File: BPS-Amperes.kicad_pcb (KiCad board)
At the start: 2 copper layers, 40 x 50 mm, 35 parts, among them J1 Conn_02x10_Odd_Even, J2 ShuntConn, J3 PassthroughConn, J4 TestConn, J5 Conn_01x02, U1 INA186A3IDDFT, U2 OPA2196, U4 REF1930AIDDCT

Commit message: Manthan Suggestions
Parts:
- turned C10 to 180 degrees
- turned C9 to 180 degrees
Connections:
- net /5V_Ext renamed /PA2
- net /Aout renamed /PA1
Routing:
- added copper zone on B.Cu, net GND
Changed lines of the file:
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@@
   (net 15 "/SPI1_MOSI")
   (net 16 "/SPI1_NSS")
-  (net 17 "/5V_Ext")
-  (net 18 "/Aout")
+  (net 17 "/PA1")
+  (net 18 "/PA2")
   (net 19 "+3V0")
   (net 20 "/RSHH")
@@
       (net 15 "/SPI1_MOSI") (pinfunction "Pin_17") (pintype "passive+no_connect"))
     (pad "18" smd rect locked (at -2.8 2.15 90) (size 0.55 1.8) (layers "F.Cu" "F.Paste" "F.Mask")
-      (net 17 "/5V_Ext") (pinfunction "Pin_18") (pintype "passive+no_connect"))
+      (net 18 "/PA2") (pinfunction "Pin_18") (pintype "passive+no_connect"))
     (pad "19" smd rect locked (at -3.6 -2.15 90) (size 0.55 1.8) (layers "F.Cu" "F.Paste" "F.Mask")
       (net 16 "/SPI1_NSS") (pinfunction "Pin_19") (pintype "passive+no_connect"))
     (pad "20" smd rect locked (at -3.6 2.15 90) (size 0.55 1.8) (layers "F.Cu" "F.Paste" "F.Mask")
-      (net 18 "/Aout") (pinfunction "Pin_20") (pintype "passive"))
+      (net 17 "/PA1") (pinfunction "Pin_20") (pintype "passive"))
     (model "${KIPRJMOD}/common/utsvt3d/connectors.3dshapes/53307-2071.stp"
       (offset (xyz 0 0 1.849999996))
@@
     (descr "Diode SMD 0805 (2012 Metric), square (rectangular) end terminal, IPC_7351 nominal, (Body size source: https://docs.google.com/spreadsheets/d/1BsfQQcO9C6DZCsRaXUlFlo91Tg2WpOkGARC1WS5S8t0/edit?usp=sharing), generated with kicad-footprint-generator")
     (tags "diode")
-    (property "Mfg" "BZX38450-C3V0X")
+    (property "Mfg" "821-BZY55B3V3RBG")
     (property "Sheetfile" "BPS-Amperes.kicad_sch")
     (property "Sheetname" "")
@@
       (stroke (width 0.1) (type solid)) (layer "B.Fab"))
     (pad "1" smd roundrect (at -0.9375 0 90) (size 0.975 1.4) (layers "B.Cu" "B.Paste" "B.Mask") (roundrect_rratio 0.25)
-      (net 18 "/Aout") (pinfunction "K") (pintype "passive"))
+      (net 17 "/PA1") (pinfunction "K") (pintype "passive"))
     (pad "2" smd roundrect (at 0.9375 0 90) (size 0.975 1.4) (layers "B.Cu" "B.Paste" "B.Mask") (roundrect_rratio 0.25)
       (net 4 "GND") (pinfunction "A") (pintype "passive"))
@@
   )
   (footprint "Capacitor_SMD:C_0805_2012Metric" (layer "B.Cu")
-    (at 146.2125 97.435)
+    (at 146.2125 97.435 180)
     (descr "Capacitor SMD 0805 (2012 Metric), square (rectangular) end terminal, IPC_7351 nominal, (Body size source: IPC-SM-782 page 76, https://www.pcb-3d.com/wordpress/wp-content/uploads/ipc-sm-782a_amendment_1_and_2.pdf, https://docs.google.com/spreadsheets/d/1BsfQQcO9C6DZCsRaXUlFlo91Tg2WpOkGARC1WS5S8t0/edit?usp=sharing), generated with kicad-footprint-generator")
     (tags "capacitor")
@@
     (property "ki_keywords" "capacitor cap")
     (attr smd)
-    (fp_text reference "C9" (at 2.4375 0.065) (layer "B.SilkS")
+    (fp_text reference "C9" (at -3.2875 0.065) (layer "B.SilkS")
         (effects (font (size 1 1) (thickness 0.15)) (justify mirror))
     )
@@
     (fp_line (start 1 0.625) (end 1 -0.625)
       (stroke (width 0.1) (type solid)) (layer "B.Fab"))
-    (pad "1" smd roundrect (at -0.95 0) (size 1 1.45) (layers "B.Cu" "B.Paste" "B.Mask") (roundrect_rratio 0.25)
+    (pad "1" smd roundrect (at -0.95 0 180) (size 1 1.45) (layers "B.Cu" "B.Paste" "B.Mask") (roundrect_rratio 0.25)
       (net 25 "+1V5") (pintype "passive"))
-    (pad "2" smd roundrect (at 0.95 0) (size 1 1.45) (layers "B.Cu" "B.Paste" "B.Mask") (roundrect_rratio 0.25)
+    (pad "2" smd roundrect (at 0.95 0 180) (size 1 1.45) (layers "B.Cu" "B.Paste" "B.Mask") (roundrect_rratio 0.25)
       (net 4 "GND") (pintype "passive"))
     (model "${KICAD6_3DMODEL_DIR}/Capacitor_SMD.3dshapes/C_0805_2012Metric.wrl"
@@
   )
   (footprint "Capacitor_SMD:C_0805_2012Metric" (layer "B.Cu")
-    (at 146.2125 100)
+    (at 146.2125 100 180)
     (descr "Capacitor SMD 0805 (2012 Metric), square (rectangular) end terminal, IPC_7351 nominal, (Body size source: IPC-SM-782 page 76, https://www.pcb-3d.com/wordpress/wp-content/uploads/ipc-sm-782a_amendment_1_and_2.pdf, https://docs.google.com/spreadsheets/d/1BsfQQcO9C6DZCsRaXUlFlo91Tg2WpOkGARC1WS5S8t0/edit?usp=sharing), generated with kicad-footprint-generator")
     (tags "capacitor")
@@
     (property "ki_keywords" "capacitor cap")
     (attr smd)
-    (fp_text reference "C10" (at 2.9375 0) (layer "B.SilkS")
+    (fp_text reference "C10" (at -3.7875 0) (layer "B.SilkS")
         (effects (font (size 1 1) (thickness 0.15)) (justify mirror))
     )
@@
     (fp_line (start 1 0.625) (end 1 -0.625)
       (stroke (width 0.1) (type solid)) (layer "B.Fab"))
-    (pad "1" smd roundrect (at -0.95 0) (size 1 1.45) (layers "B.Cu" "B.Paste" "B.Mask") (roundrect_rratio 0.25)
+    (pad "1" smd roundrect (at -0.95 0 180) (size 1 1.45) (layers "B.Cu" "B.Paste" "B.Mask") (roundrect_rratio 0.25)
       (net 25 "+1V5") (pintype "passive"))
-    (pad "2" smd roundrect (at 0.95 0) (size 1 1.45) (layers "B.Cu" "B.Paste" "B.Mask") (roundrect_rratio 0.25)
+    (pad "2" smd roundrect (at 0.95 0 180) (size 1 1.45) (layers "B.Cu" "B.Paste" "B.Mask") (roundrect_rratio 0.25)
       (net 4 "GND") (pintype "passive"))
     (model "${KICAD6_3DMODEL_DIR}/Capacitor_SMD.3dshapes/C_0805_2012Metric.wrl"
@@
       (net 32 "Net-(U2B--)") (pintype "passive"))
     (pad "2" smd roundrect (at 0.9125 0) (size 1.025 1.4) (layers "B.Cu" "B.Paste" "B.Mask") (roundrect_rratio 0.243902)
-      (net 18 "/Aout") (pintype "passive"))
+      (net 17 "/PA1") (pintype "passive"))
     (model "${KICAD6_3DMODEL_DIR}/Resistor_SMD.3dshapes/R_0805_2012Metric.wrl"
       (offset (xyz 0 0 0))
@@
       (stroke (width 0.1) (type solid)) (layer "B.Fab"))
     (pad "1" thru_hole rect (at 0 0 90) (size 1.7 1.7) (drill 1) (layers "*.Cu" "*.Mask")
-      (net 18 "/Aout") (pinfunction "1") (pintype "passive"))
+      (net 17 "/PA1") (pinfunction "1") (pintype "passive"))
     (model "${KICAD6_3DMODEL_DIR}/Connector_PinHeader_2.54mm.3dshapes/PinHeader_1x01_P2.54mm_Horizontal.wrl"
       (offset (xyz 0 0 0))
@@
     (property "ki_keywords" "dual opamp low-power")
     (attr smd)
-    (fp_text reference "U2" (at 0.025 -3.345 270) (layer "B.SilkS")
+    (fp_text reference "U2" (at 0.025 -3.345 90) (layer "B.SilkS")
         (effects (font (size 1 1) (thickness 0.15)) (justify mirror))
     )
@@
       (stroke (width 0.1) (type solid)) (layer "B.Fab"))
     (pad "1" smd roundrect (at -0.95 0 90) (size 1 1.45) (layers "B.Cu" "B.Paste" "B.Mask") (roundrect_rratio 0.25)
-      (net 18 "/Aout") (pintype "passive"))
+      (net 17 "/PA1") (pintype "passive"))
     (pad "2" smd roundrect (at 0.95 0 90) (size 1 1.45) (layers "B.Cu" "B.Paste" "B.Mask") (roundrect_rratio 0.25)
       (net 4 "GND") (pintype "passive"))
@@
     (style (thickness 0.1) (arrow_length 1.27) (text_position_mode 0) (extension_height 0.58642) (extension_offset 0.5) keep_text_aligned)
   )
+  (zone (net 4) (net_name "GND") (layer "B.Cu") (hatch edge 0.5)
+    (connect_pads (clearance 0.25))
+    (min_thickness 0.25) (filled_areas_thickness no)
+    (fill yes (thermal_gap 0.5) (thermal_bridge_width 0.5))
+    (polygon
+      (pts
+        (xy 130 66)
+        (xy 170 66)
+        (xy 170 116)
+        (xy 130 116)
+      )
+    )
+  )
   (group "" (id 9c716276-2a82-4619-908a-de798b1d9a88)

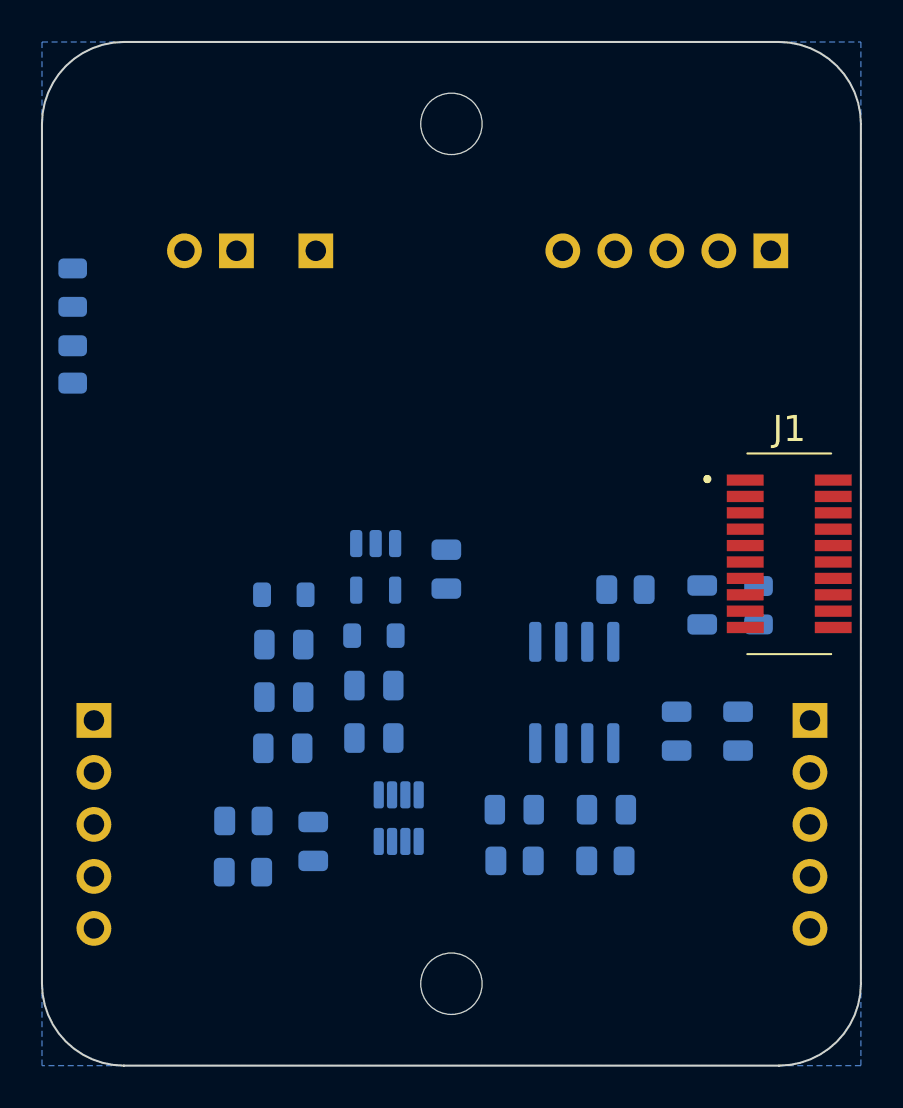
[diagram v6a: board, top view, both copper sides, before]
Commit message: Initial tracing, improvements to come via Tianda's review
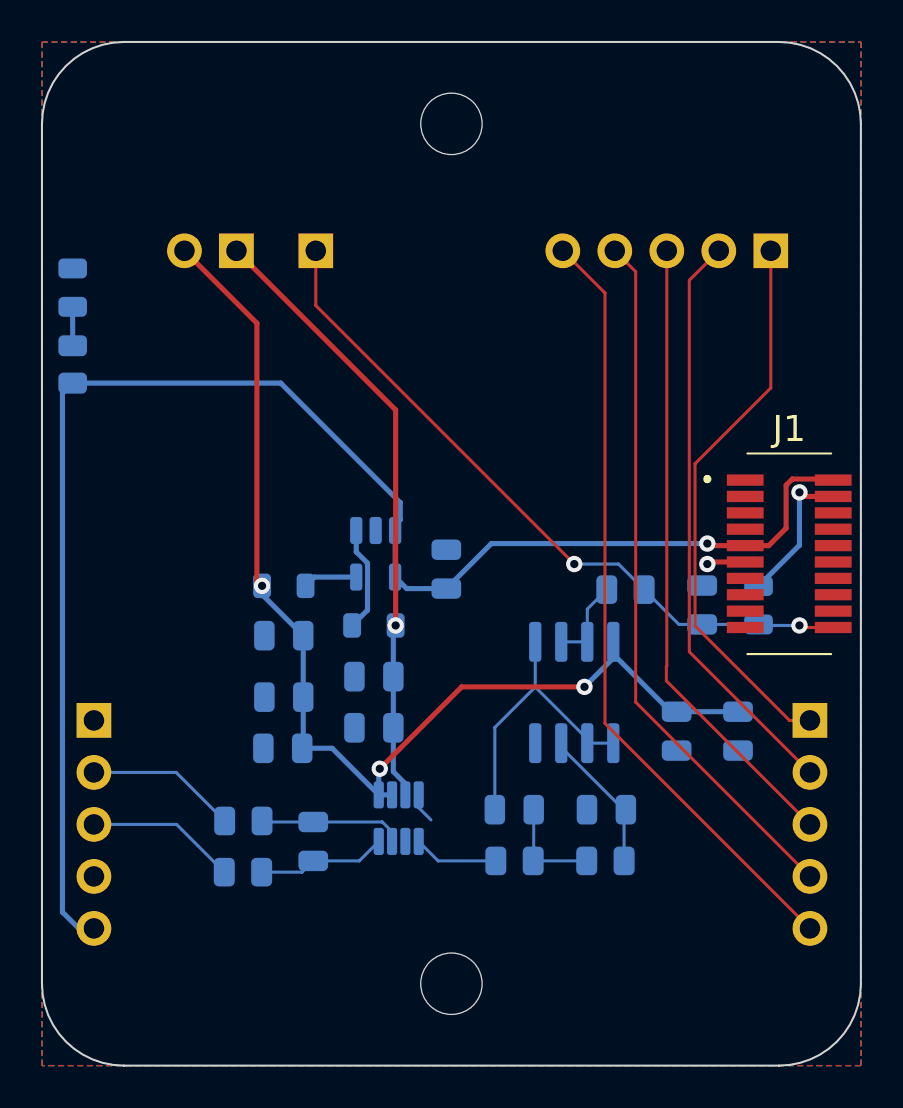
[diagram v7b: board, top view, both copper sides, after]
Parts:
- moved LOGO1 0.71 mm to (161.0, 112.0)
- moved U4 0.64 mm to (146.3, 91.0)
- moved C10 0.50 mm to (146.2, 99.5)
- moved FB1 0.50 mm to (146.2, 94.5)
- moved C11 0.44 mm to (141.8, 95.0)
- moved C9 0.44 mm to (146.2, 97.0)
- moved FB2 0.44 mm to (141.8, 92.6)
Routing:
- net +3.3V: track 0.00 -> 75.3 mm, vias 0 -> 1
- net +3V0: track 0.00 -> 55.7 mm, vias 0 -> 3
- net /V-: track 0.00 -> 38.1 mm
- net /V+: track 0.00 -> 34.5 mm
- net /PA1: track 0.00 -> 34.5 mm, vias 0 -> 2
- net /TEST: track 0.00 -> 30.9 mm
- net +1V5: track 0.00 -> 30.1 mm, vias 0 -> 1
- net /SHUNT: track 0.00 -> 28.5 mm
- net /NOTCON: track 0.00 -> 27.4 mm
- net GND: track 0.00 -> 18.2 mm, vias 0 -> 2
- net Net-(U2A--): track 0.00 -> 14.1 mm
- net Net-(J2-Pin_2): track 0.00 -> 7.37 mm
- net Net-(U2A-+): track 0.00 -> 7.16 mm
- net /RSHH: track 0.00 -> 7.04 mm
- net /RSHL: track 0.00 -> 6.34 mm
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- added copper zone on F.Cu, net GND

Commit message: The Thickening
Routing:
- net /NOTCON: track 27.4 -> 37.1 mm
- net /SHUNT: track 28.5 -> 36.2 mm
- net GND: track 18.2 -> 11.1 mm, vias 2 -> 1
- net /TEST: track 30.9 -> 36.9 mm
- net /V+: track 34.5 -> 37.2 mm
- net /PA1: track 34.5 -> 35.7 mm
- net +3V0: track 55.7 -> 55.0 mm
